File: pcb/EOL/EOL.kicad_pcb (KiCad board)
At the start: 2 copper layers, 51 x 47.2 mm, 35 parts, among them J1 Conn_01x06, SW1 Slide_DPDT, SW2 Slide_DPDT, SW3 Slide_DPDT, SW4 Slide_DPDT, SW5 SW_Push_DPDT, SW6 SW_Push_DPDT, SW7 SW_Push_DPDT

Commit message: Updated Board labels. Made them bigger 👁️
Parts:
- removed kibuzzard-62360F8D (x2), kibuzzard-62360FC7 (x2), kibuzzard-62361022 (x3), kibuzzard-62361049 (x3): G***, label
- removed kibuzzard-6255E20F: G***, kibuzzard-6255E20F
- removed kibuzzard-6255E264: G***, kibuzzard-6255E264
- removed kibuzzard-6255E2F9 (x3): G***, kibuzzard-6255E2F9
- removed kibuzzard-6255E32D: G***, kibuzzard-6255E32D
- added kibuzzard-6481E1FA: G***, kibuzzard-6481E1FA, F.Cu at (27.0, 30.0)
- added kibuzzard-6481E1FA: G***, kibuzzard-6481E1FA, F.Cu at (49.0, 30.0)
- added kibuzzard-6481E268: G***, kibuzzard-6481E268, F.Cu at (57.5, 29.1)
- added kibuzzard-6481E268: G***, kibuzzard-6481E268, F.Cu at (37.5, 29.1)
- added kibuzzard-6481E2B4: G***, kibuzzard-6481E2B4, F.Cu at (50.9, 38.5)
- added kibuzzard-6481E2F6: G***, kibuzzard-6481E2F6, F.Cu at (24.0, 39.3)
- added kibuzzard-6481E2F6: G***, kibuzzard-6481E2F6, F.Cu at (35.0, 39.3)
- added kibuzzard-6481E2F6: G***, kibuzzard-6481E2F6, F.Cu at (46.0, 39.3)
- added kibuzzard-6481E3F6: G***, kibuzzard-6481E3F6, F.Cu at (56.1, 49.0)
- added kibuzzard-6481E412: G***, kibuzzard-6481E412, F.Cu at (56.1, 43.9)
- added kibuzzard-6481E4F7: G***, kibuzzard-6481E4F7, F.Cu at (18.1, 42.0)
- added kibuzzard-6481E55F: G***, kibuzzard-6481E55F, F.Cu at (18.1, 31.7)
- moved R4 1.15 mm to (50.9, 40.4)
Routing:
- net Net-(R2-Pad1): track 6.76 -> 5.61 mm
- net Net-(R4-Pad1): track 19.8 -> 20.5 mm
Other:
- board text added: "Nuno Nogueira Stockholm 05-23 v1.0"
- board text removed: "Nuno Nogueira Stockholm 03-22"

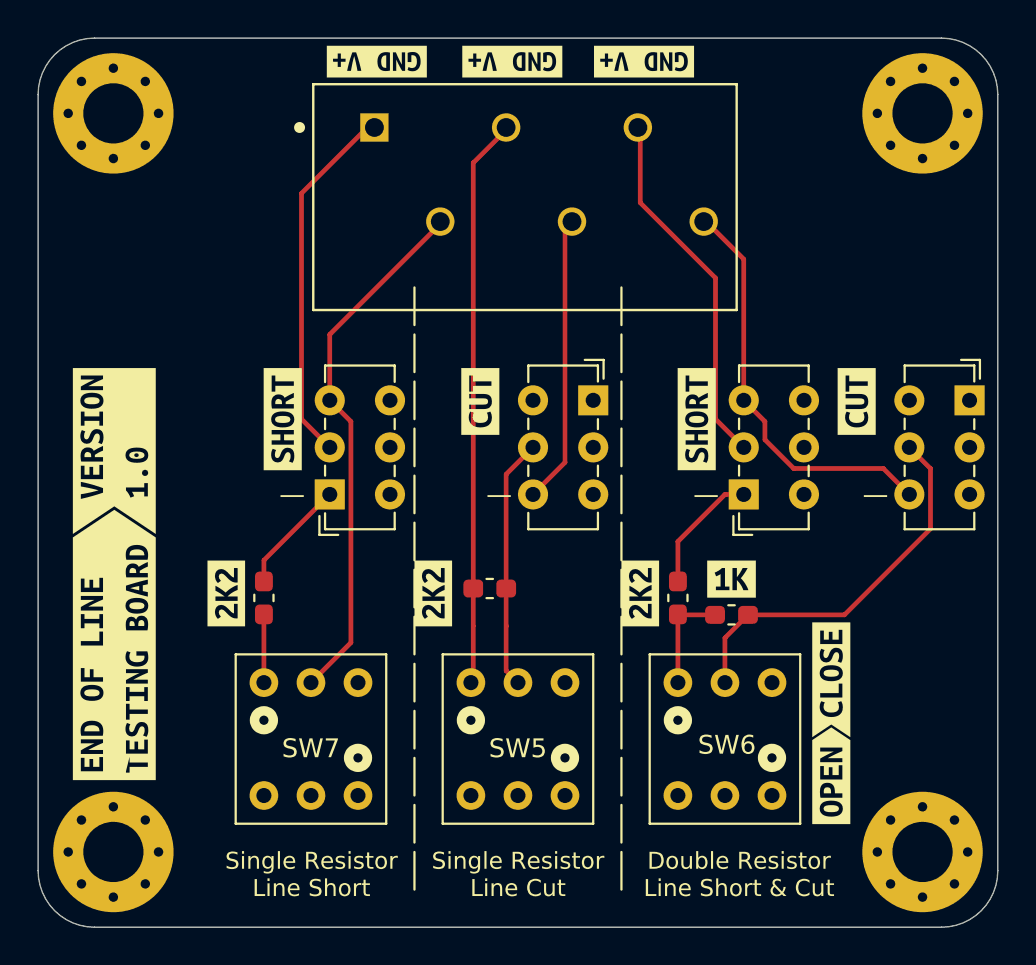
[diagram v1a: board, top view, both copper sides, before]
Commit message: Replace the terminal footprint for a screw terminal. Added the LCSC unique ids to ease the process of ordering a pcb.
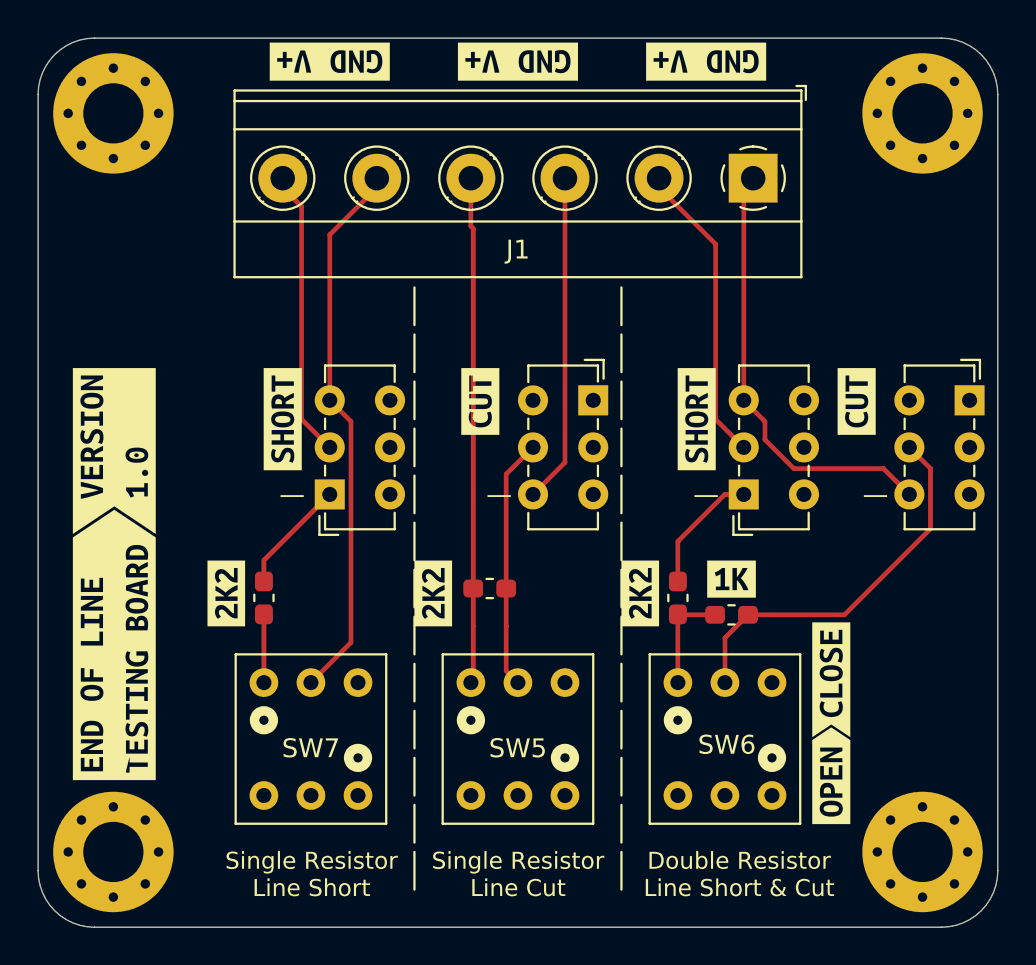
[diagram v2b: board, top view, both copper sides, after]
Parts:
- removed kibuzzard-624DDF7A (x3): G***, kibuzzard-624DDF7A
- added kibuzzard-6482D2A7: G***, kibuzzard-6482D2A7, F.Cu at (39.5, 11.0)
- added kibuzzard-6482D2A7: G***, kibuzzard-6482D2A7, F.Cu at (49.5, 11.0)
- added kibuzzard-6482D2A7: G***, kibuzzard-6482D2A7, F.Cu at (29.5, 11.0)
- J1: footprint External:PHOENIX_1985234 -> TerminalBlock_Phoenix:TerminalBlock_Phoenix_MKDS-1,5-6_1x06_P5.00mm_Horizontal
- R1, R3: value 2k -> 2k2
- R2: value 1k -> 2k2
- R4: value 2k -> 1k
- moved J1 20.3 mm to (52.0, 17.2), turned to 180 degrees
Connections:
- J1 pad 1: SLS1 -> IN3
- J1 pad 2: IN1 -> DL
- J1 pad 3: SLC1 -> IN2
- J1 pad 4: IN2 -> SLC1
- J1 pad 5: DL -> IN1
- J1 pad 6: IN3 -> SLS1
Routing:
- net SLS1: track 19.1 -> 14.8 mm
- net SLC1: track 30.2 -> 26.3 mm
- net DL: track 19.3 -> 15.7 mm
- net IN2: track 15.4 -> 17.0 mm
- net IN3: track 21.8 -> 22.9 mm
